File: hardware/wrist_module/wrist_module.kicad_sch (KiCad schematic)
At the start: 16 parts, among them J1 +3V3 Battery Connector, J2 Conn_02x05_Row_Letter_First, SW1 Reset SW, U1 XIAO ESP32C3, U2 ULN2003A

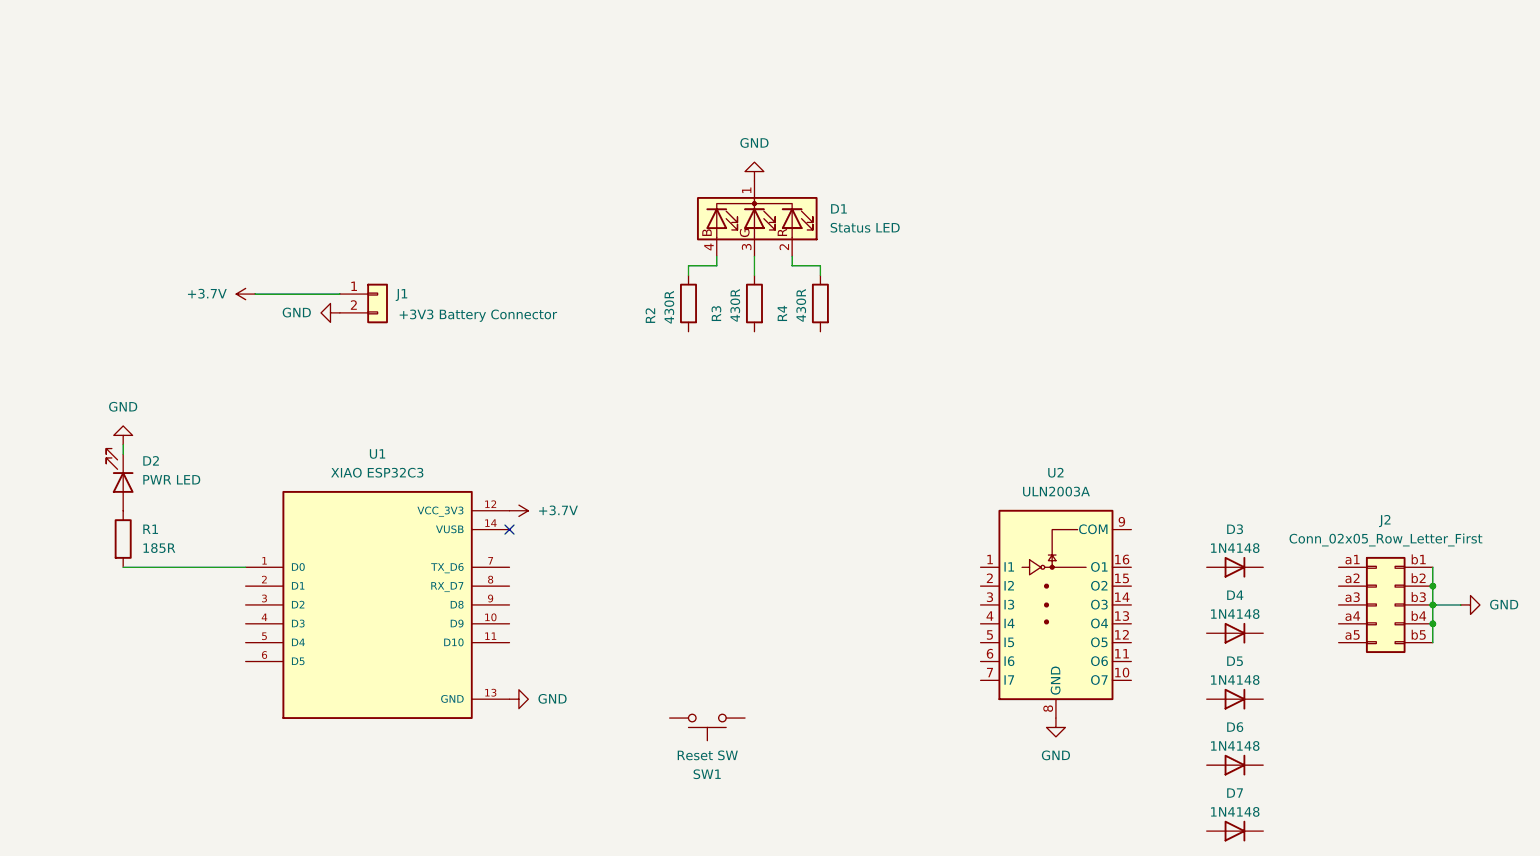
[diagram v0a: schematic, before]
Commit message: Update wrist module schematic and PCB, add hardware README
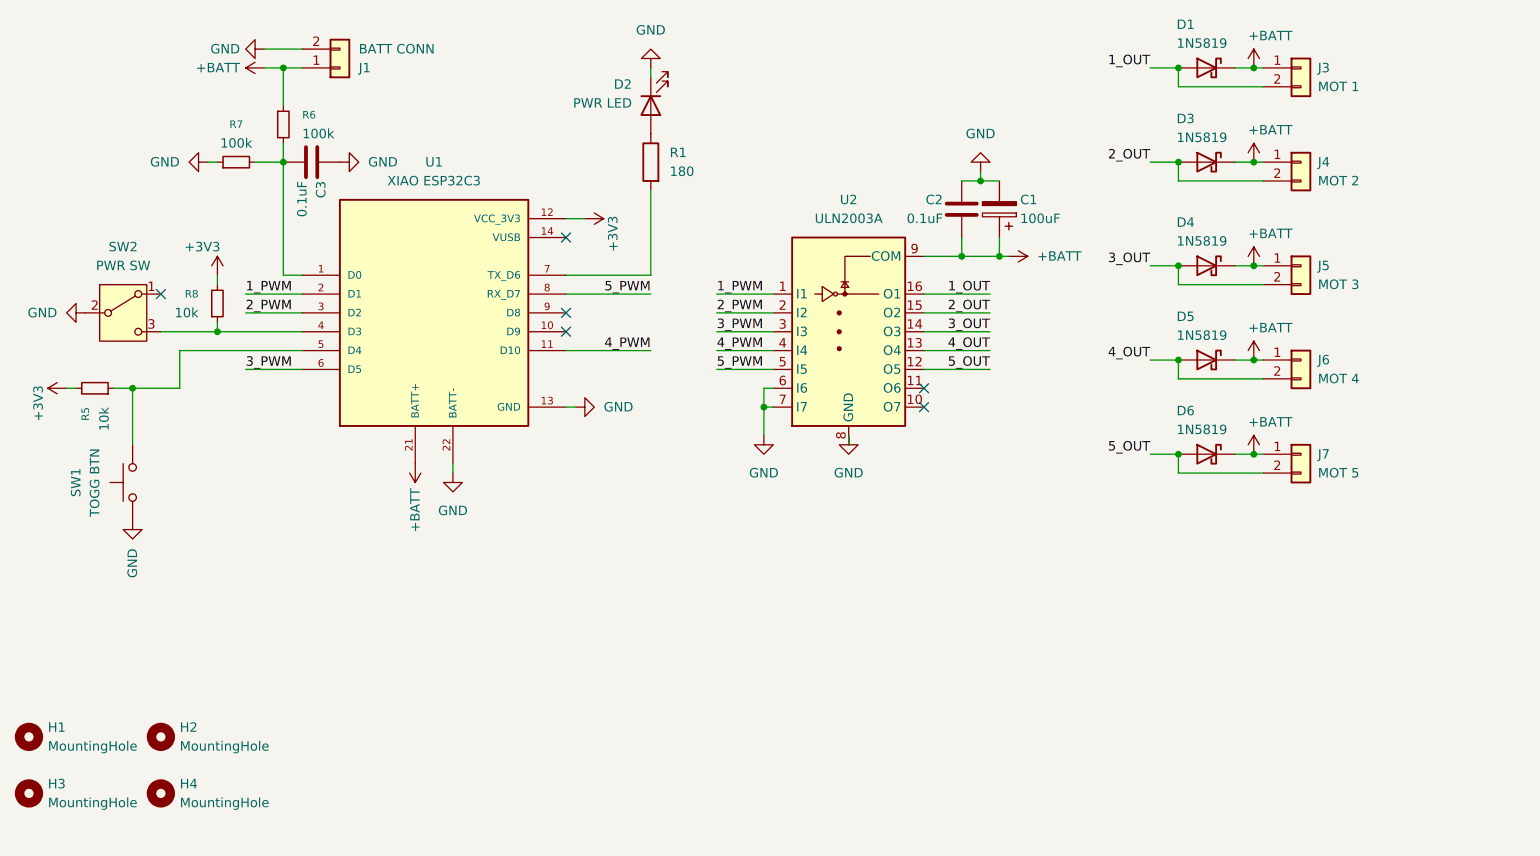
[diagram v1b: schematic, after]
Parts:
- removed D1: Status LED, Display:NHD-C0220BiZ-FSRGB, symbol Device:LED_KRGB
- removed D3, D4, D5, D6, D7: 1N4148, Diode_THT:D_DO-35_SOD27_P7.62mm_Horizontal, symbol Diode:1N4148
- removed J2: Conn_02x05_Row_Letter_First, Package_SO:SOIC-8_3.9x4.9mm_P1.27mm, symbol Connector_Generic:Conn_02x05_Row_Letter_First
- removed R2, R3, R4: 430R, Package_DIP:DIP-8_W7.62mm, symbol Device:R
- added C1: 100uF, Capacitor_THT:CP_Radial_D8.0mm_P2.50mm, symbol Device:C_Polarized
- added C2, C3: 0.1uF, Capacitor_THT:C_Disc_D3.8mm_W2.6mm_P2.50mm, symbol Device:C
- added D1, D3, D4, D5, D6: 1N5819, Diode_THT:D_DO-41_SOD81_P10.16mm_Horizontal, symbol Diode:1N5819
- added H1, H2, H3, H4: MountingHole, MountingHole:MountingHole_2.2mm_M2_ISO7380, symbol Mechanical:MountingHole
- added J3: MOT 1, Connector_JST:JST_PH_B2B-PH-K_1x02_P2.00mm_Vertical, symbol Connector_Generic:Conn_01x02
- added J4: MOT 2, Connector_JST:JST_PH_B2B-PH-K_1x02_P2.00mm_Vertical, symbol Connector_Generic:Conn_01x02
- added J5: MOT 3, Connector_JST:JST_PH_B2B-PH-K_1x02_P2.00mm_Vertical, symbol Connector_Generic:Conn_01x02
- added J6: MOT 4, Connector_JST:JST_PH_B2B-PH-K_1x02_P2.00mm_Vertical, symbol Connector_Generic:Conn_01x02
- added J7: MOT 5, Connector_JST:JST_PH_B2B-PH-K_1x02_P2.00mm_Vertical, symbol Connector_Generic:Conn_01x02
- added R5, R8: 10k, Resistor_THT:R_Axial_DIN0207_L6.3mm_D2.5mm_P7.62mm_Horizontal, symbol Device:R_Small
- added R6, R7: 100k, Resistor_THT:R_Axial_DIN0207_L6.3mm_D2.5mm_P7.62mm_Horizontal, symbol Device:R_Small
- added SW2: PWR SW, Connector_JST:JST_PH_B3B-PH-K_1x03_P2.00mm_Vertical, symbol Switch:SW_SPDT
- D2: footprint (none) -> LED_THT:LED_D5.0mm
- J1: value +3V3 Battery Connector -> BATT CONN; footprint Package_DIP:DIP-20_W7.62mm -> Connector_JST:JST_PH_B2B-PH-K_1x02_P2.00mm_Vertical
- R1: value 185R -> 180; footprint Package_DIP:DIP-8_W7.62mm -> Resistor_THT:R_Axial_DIN0207_L6.3mm_D2.5mm_P7.62mm_Horizontal
- SW1: value Reset SW -> TOGG BTN; footprint Package_SON:WSON-8-1EP_6x5mm_P1.27mm_EP3.4x4mm -> Button_Switch_THT:SW_PUSH_6mm
- U1: footprint 113991054:MODULE_113991054 -> XIAO Library:XIAO-ESP32-C3-DIP-SMD
- U2: footprint (none) -> Package_DIP:DIP-16_W7.62mm_LongPads
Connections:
- net GND: now also SW1.2, U1.22 (BATT-), U2.6 (I6), U2.7 (I7), C1.2, C2.1, C3.1, R7.1, SW2.2 (B)
- net 1_PWM: now reaches U2.1 (I1)
- net 1_PWM: now also U1.2 (D1)
- net 5_OUT: now reaches U2.12 (O5)
- net 5_OUT: now also D6.2 (A), J7.2 (Pin_2)
- net 4_OUT: now reaches U2.13 (O4)
- net 4_OUT: now also D5.2 (A), J6.2 (Pin_2)
- net 3_OUT: now reaches U2.14 (O3)
- net 3_OUT: now also D4.2 (A), J5.2 (Pin_2)
- net 2_OUT: now reaches U2.15 (O2)
- net 2_OUT: now also D3.2 (A), J4.2 (Pin_2)
- net 1_OUT: now reaches U2.16 (O1)
- net 1_OUT: now also D1.2 (A), J3.2 (Pin_2)
- net 2_PWM: now reaches U2.2 (I2)
- net 2_PWM: now also U1.3 (D2)
- net 3_PWM: now reaches U2.3 (I3)
- net 3_PWM: now also U1.6 (D5)
- net 4_PWM: now reaches U2.4 (I4)
- net 4_PWM: now also U1.11 (D10)
- net 5_PWM: now reaches U2.5 (I5)
- net 5_PWM: now also U1.8 (RX_D7)
- net +BATT: now reaches U2.9 (COM)
- net +BATT: now also J1.1 (Pin_1), U1.21 (BATT+), C1.1, C2.2, D1.1 (K), D3.1 (K), D4.1 (K), D5.1 (K), D6.1 (K), J3.1 (Pin_1), J4.1 (Pin_1), J5.1 (Pin_1), J6.1 (Pin_1), J7.1 (Pin_1), R6.1
- net at U1.1 (D0): now also C3.2, R6.2, R7.2; no longer R1.2
- net at U1.4 (D3): now also R8.1, SW2.3 (C)
- net at U1.5 (D4): now also SW1.1, R5.1
- net at U1.7 (TX_D6): now also R1.2
- net +3.7V renamed +3V3
- net +3V3: now also R5.2, R8.2; no longer J1.1 (Pin_1)
- no-connect marks 1 -> 6
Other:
- company: (none) -> UCSC - CSE 115A
- title: (none) -> DareDevil - Wrist Module
- moved on the sheet: U2
